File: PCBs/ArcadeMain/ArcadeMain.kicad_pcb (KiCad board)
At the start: 4 copper layers, 81.7 x 163.3 mm, 12 parts, among them J1 Conn_01x17_Male, J2 Conn_01x17_Male, J21 USB_B_Micro, J23 Conn_02x22_Top_Bottom, J24 USB_B_Micro, J3 Screw_Terminal_01x12, J4 Conn_01x17_Male, J5 Conn_01x17_Male

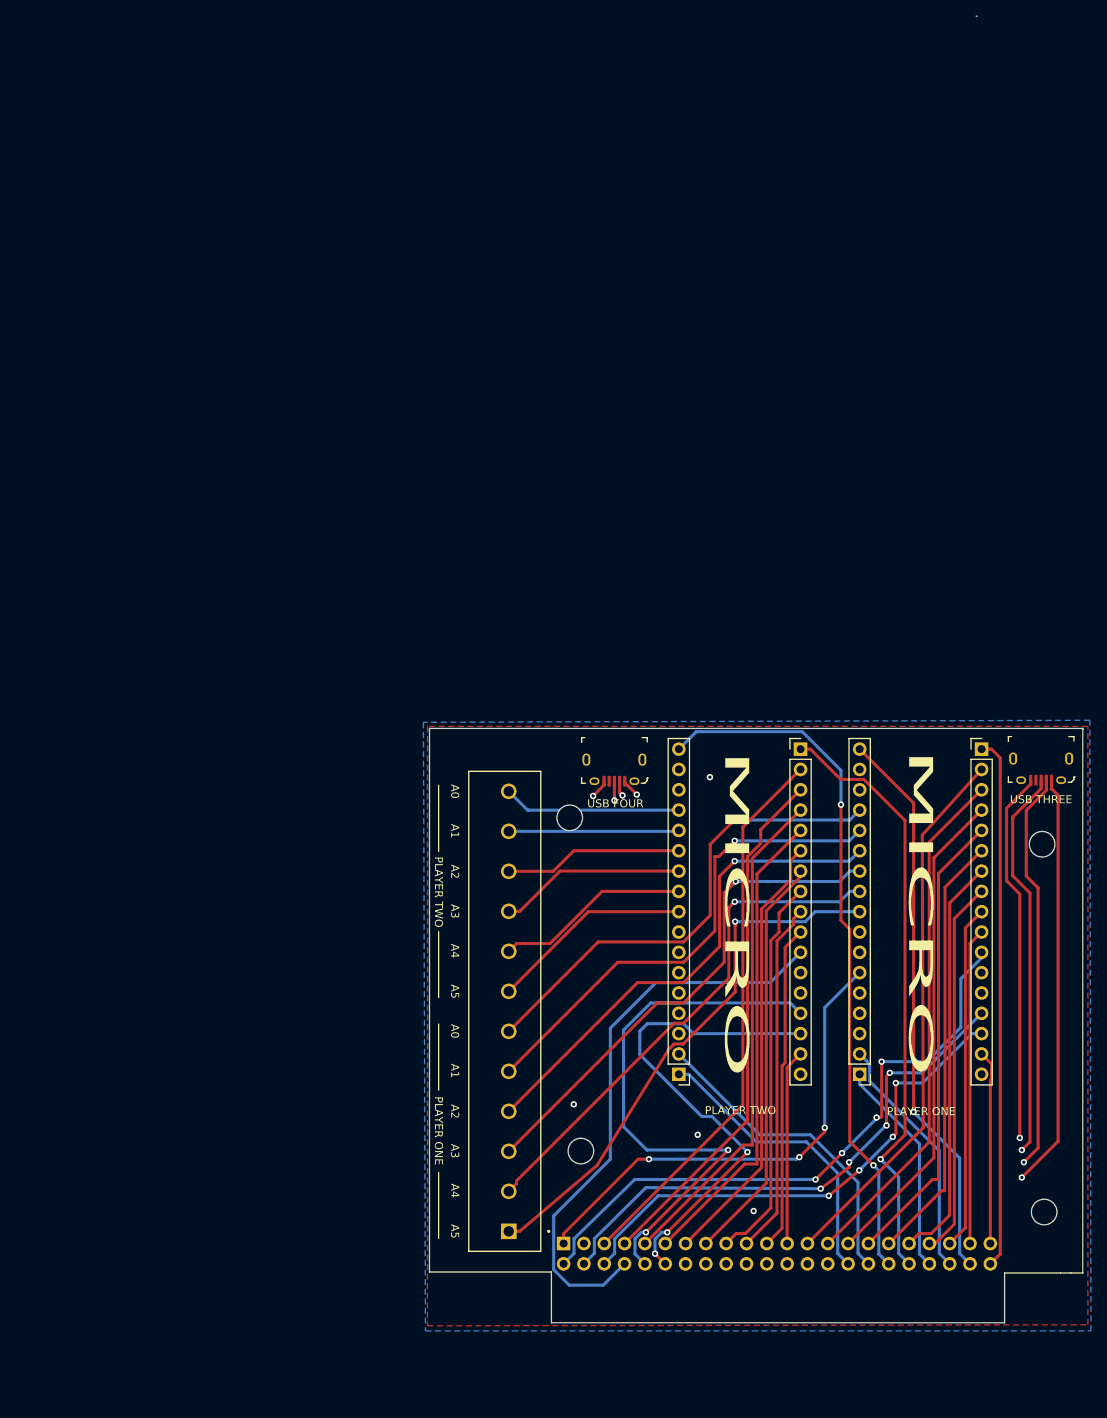
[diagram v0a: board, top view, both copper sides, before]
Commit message: v2 PCB revisions: switch to ribbon cable rather than PCB edge, add DIP switch for panel identifications
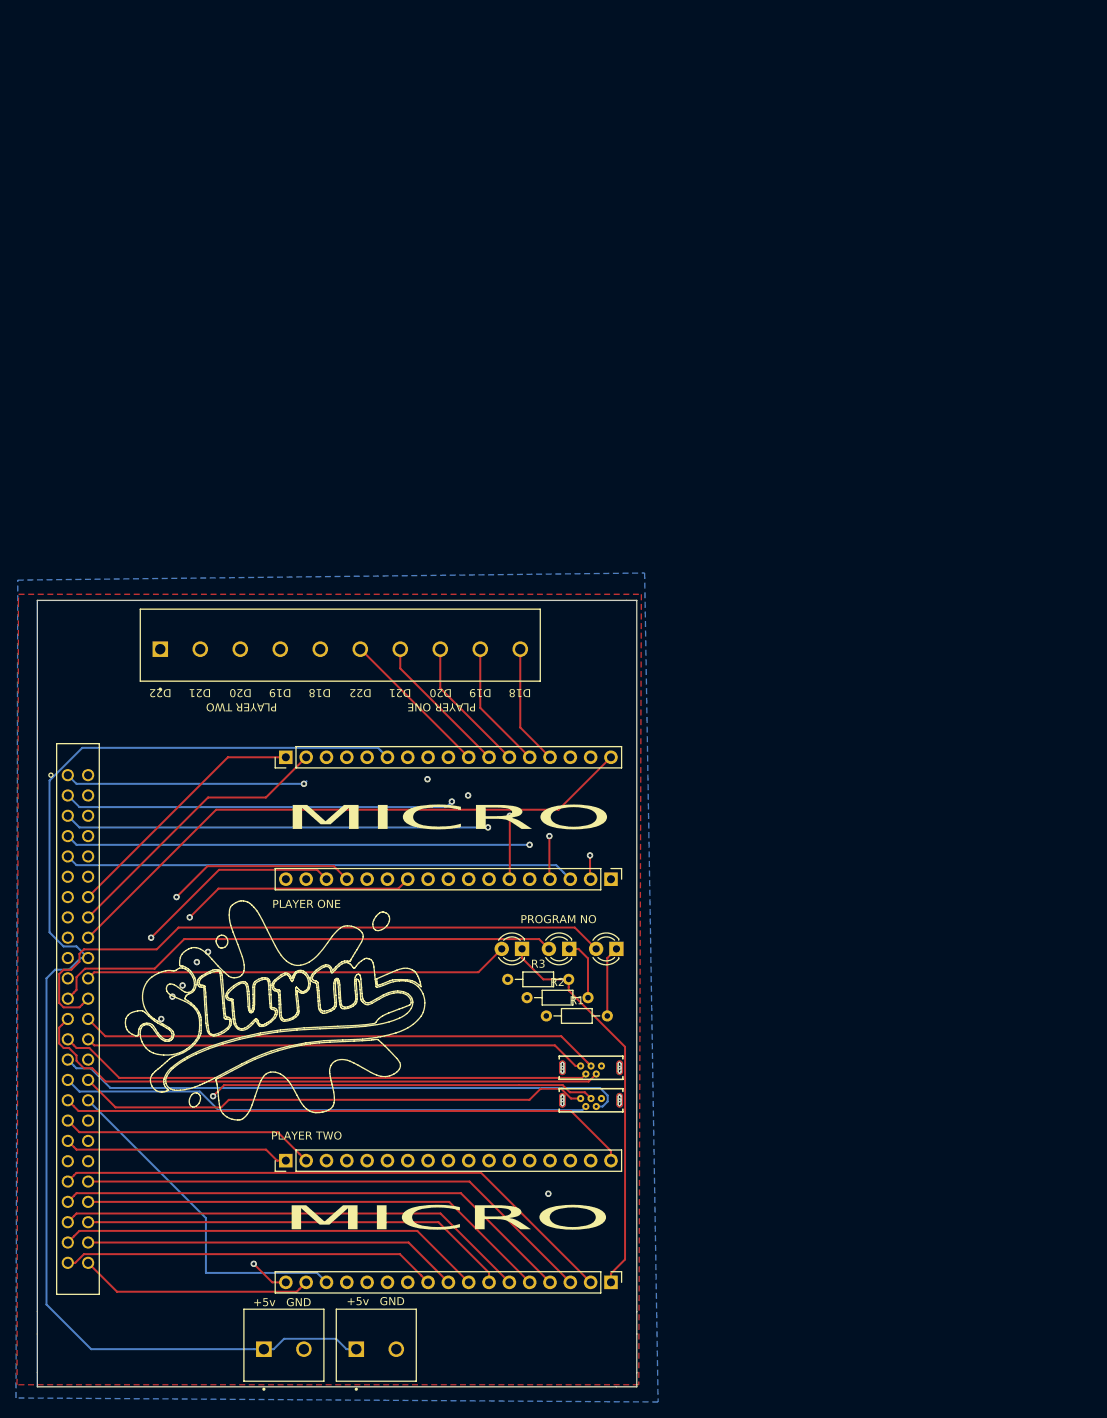
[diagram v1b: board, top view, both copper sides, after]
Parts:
- removed 4 (x4): MountingHole_3.2mm_M3, MountingHole:MountingHole_3.2mm_M3
- removed J23: Conn_02x22_Top_Bottom, Connector_PinHeader_2.54mm:PinHeader_2x22_P2.54mm_Horizontal
- added D1: LED, LED_THT:LED_D3.0mm, F.Cu at (130.8, 77.9)
- added D2: LED, LED_THT:LED_D3.0mm, F.Cu at (124.9, 77.9)
- added D3: LED, LED_THT:LED_D3.0mm, F.Cu at (119.0, 77.9)
- added J6: SBH11-PBPC-D25-ST-BK, ul_SBH11PBPCD25STBK:SBH11-PBPC-D25-ST-BK, F.Cu at (62.2, 56.1)
- added J7: Screw_Terminal_01x10, TB001-500-08BE:CUI_TB001-500-02BE, F.Cu at (86.7, 127.9)
- added J8: Screw_Terminal_01x10, TB001-500-08BE:CUI_TB001-500-02BE, F.Cu at (98.3, 127.9)
- added R1: 220, Resistor_THT:R_Axial_DIN0204_L3.6mm_D1.6mm_P7.62mm_Horizontal, F.Cu at (122.0, 86.2)
- added R2: 220, Resistor_THT:R_Axial_DIN0204_L3.6mm_D1.6mm_P7.62mm_Horizontal, F.Cu at (119.6, 83.9)
- added R3: 220, Resistor_THT:R_Axial_DIN0204_L3.6mm_D1.6mm_P7.62mm_Horizontal, F.Cu at (117.2, 81.7)
- J21, J24: footprint digikey-footprints:USB_Micro_B_Female_10118194-0001LF -> ryan-common-library:GCT_USB3131-XX-0230-X_REVB
- J3: value Screw_Terminal_01x12 -> Screw_Terminal_01x10; footprint TB001-500-12BE:CUI_TB001-500-12BE -> TB001-500-10BE:CUI_TB001-500-10BE
- moved J3 84.8 mm to (73.8, 40.4), turned to 0 degrees
- moved J1 81.9 mm to (89.5, 53.9), turned to 90 degrees
- moved J5 70.7 mm to (130.1, 119.5), turned to 270 degrees
- moved J21 66.8 mm to (127.6, 92.7), turned to 0 degrees
- moved J4 50.3 mm to (89.5, 104.3), turned to 90 degrees
- moved J2 49.1 mm to (130.1, 69.1), turned to 270 degrees
- moved J24 40.0 mm to (127.6, 96.8), turned to 0 degrees
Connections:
- J1 pad 6: /+5v -> /+5V
- J21 pad 1: /USBTHREE-R -> /USB-5
- J21 pad 2: /USBTHREE-W -> /USB-6
- J21 pad 3: /USBTHREE-G -> /USB-7
- J21 pad 4: Net-(J21-Pad4) -> /USB-8
- J21 pad 5: /USBTHREE-B -> /GND
- J24 pad 1: /USBFOUR-R -> /USB-1
- J24 pad 2: /USBFOUR-W -> /USB-2
- J24 pad 3: /USBFOUR-G -> /USB-3
- J24 pad 4: Net-(J24-Pad4) -> /USB-4
- J24 pad 5: /USBFOUR-B -> /GND
- J3 pad 1: /1-A5-D23 -> /2-A4-D22
- J3 pad 10: /2-A2-D20 -> /1-A0-D18
- J3 pad 2: /1-A4-D22 -> /2-A3-D21
- J3 pad 3: /1-A3-D21 -> /2-A2-D20
- J3 pad 4: /1-A2-D20 -> /2-A1-D19
- J3 pad 5: /1-A1-D19 -> /2-A0-D18
- J3 pad 6: /1-A0-D18 -> /1-A4-D22
- J3 pad 7: /2-A5-D23 -> /1-A3-D21
- J3 pad 8: /2-A4-D22 -> /1-A2-D20
- J3 pad 9: /2-A3-D21 -> /1-A1-D19
- J4 pad 9: /2-A5-D23 -> /1-A5-D23
- J5 pad 1: /2-A11-D12 -> /1-A11-D12
- J5 pad 17: /2-MOSI-D16 -> /1-MOSI-D16
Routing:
- net /+5V: track 0.00 -> 158.7 mm
- net /1-MOSI-D16: track 0.00 -> 102.9 mm, vias 0 -> 1
- net /USBTHREE-G: track 86.0 -> 0.00 mm, vias 1 -> 0
- net /USBTHREE-B: track 85.9 -> 0.00 mm, vias 1 -> 0
- net /USBTHREE-W: track 83.6 -> 0.00 mm, vias 1 -> 0
- net /USBTHREE-R: track 81.3 -> 0.00 mm, vias 1 -> 0
- net /DIP-1: track 0.00 -> 79.1 mm
- net /2-A1-D19: track 21.5 -> 97.1 mm, vias 0 -> 1
- net /2-A0-D18: track 22.3 -> 97.2 mm, vias 0 -> 1
- net /2-A11-D12: track 74.9 -> 0.00 mm, vias 1 -> 0
- net /USB-8: track 0.00 -> 73.4 mm
- net /2-A2-D20: track 22.3 -> 94.9 mm, vias 0 -> 1
- net /USB-4: track 0.00 -> 71.8 mm
- net /2-A3-D21: track 23.3 -> 93.1 mm, vias 0 -> 1
- net /2-A4-D22: track 24.4 -> 92.0 mm, vias 0 -> 1
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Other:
- board size 81.7 x 163.3 mm -> 74.9 x 98.3 mm
- board text added: "+5v GND"
- board text added: "BATEMAN - ARCADE MAIN v2.0 2020-07"
- board text added: "D18"
- board text added: "D19"
- board text added: "D20"
- board text added: "D21"
- board text added: "D22"
- board text added: "PROGRAM NO"
- board text removed: "+5v"
- board text removed: "A0"
- board text removed: "A1"
- board text removed: "A2"
- board text removed: "A3"
- board text removed: "A4"
- board text removed: "A5"
- board text removed: "BATEMAN - ARCADE MAIN PANEL v1.0 2020-06"
- board text removed: "Connector"
- board text removed: "GND"
- board text removed: "USB FOUR"
- board text removed: "USB THREE"
